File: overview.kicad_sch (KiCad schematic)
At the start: 0 parts

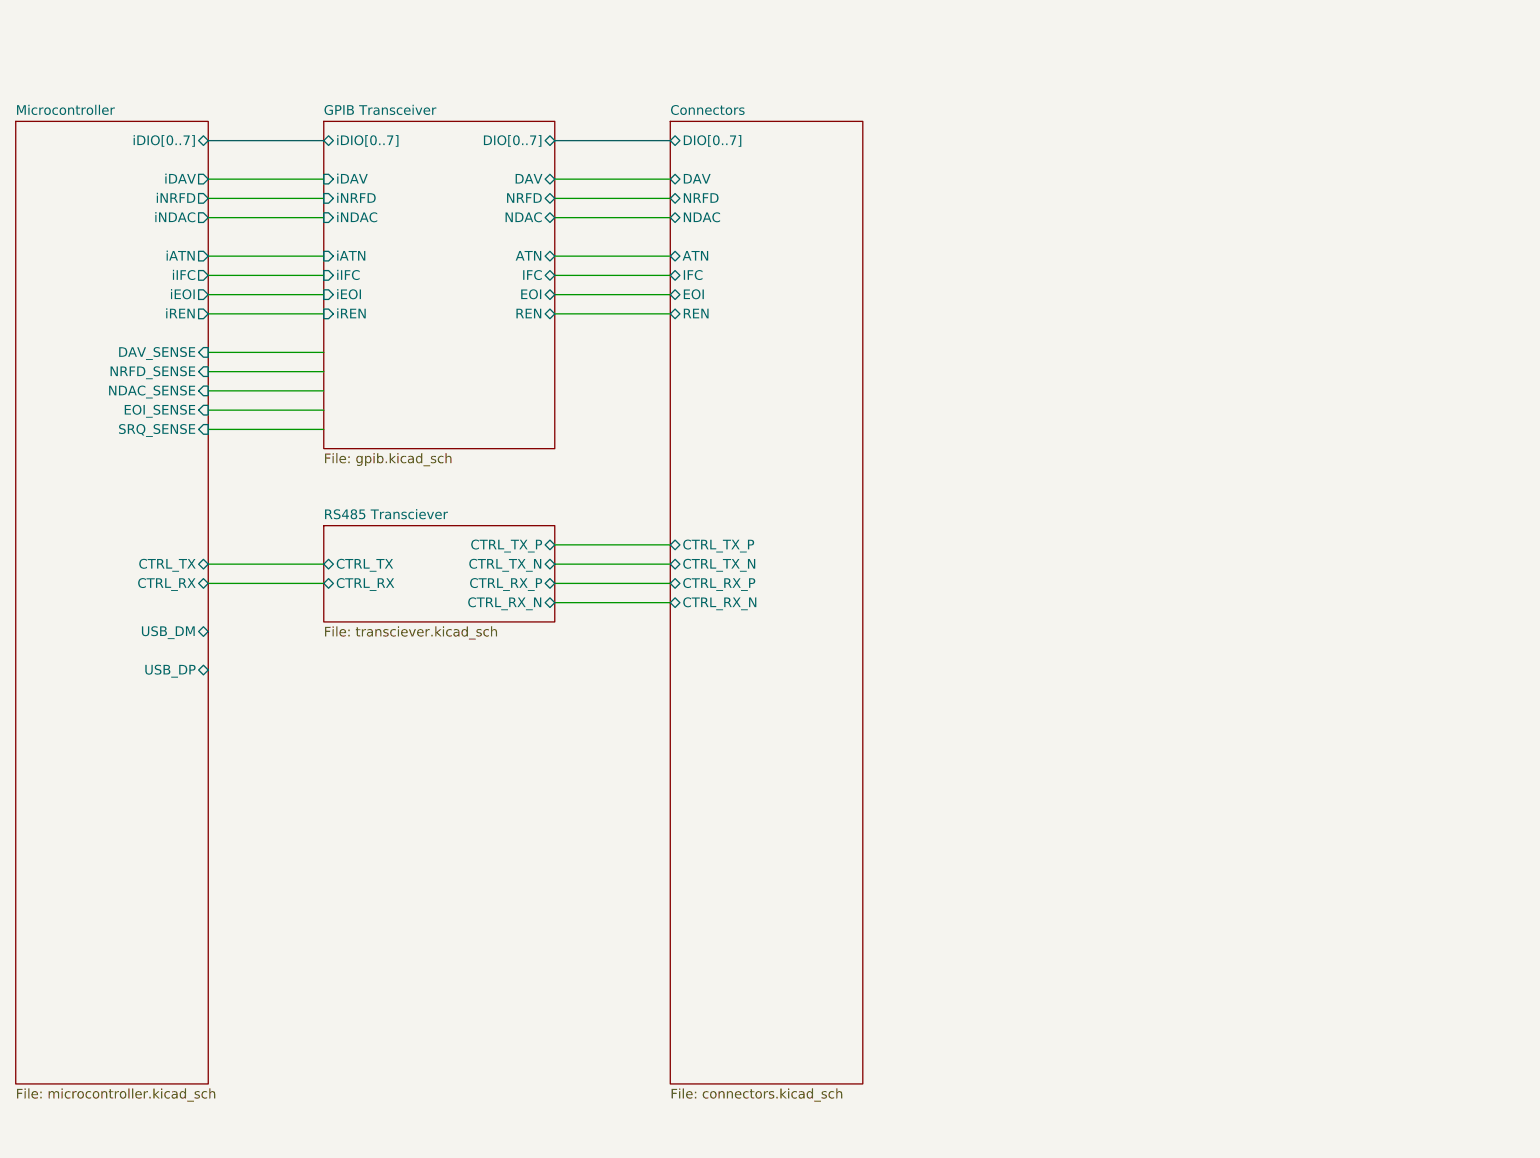
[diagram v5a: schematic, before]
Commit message: Add GPIB interface
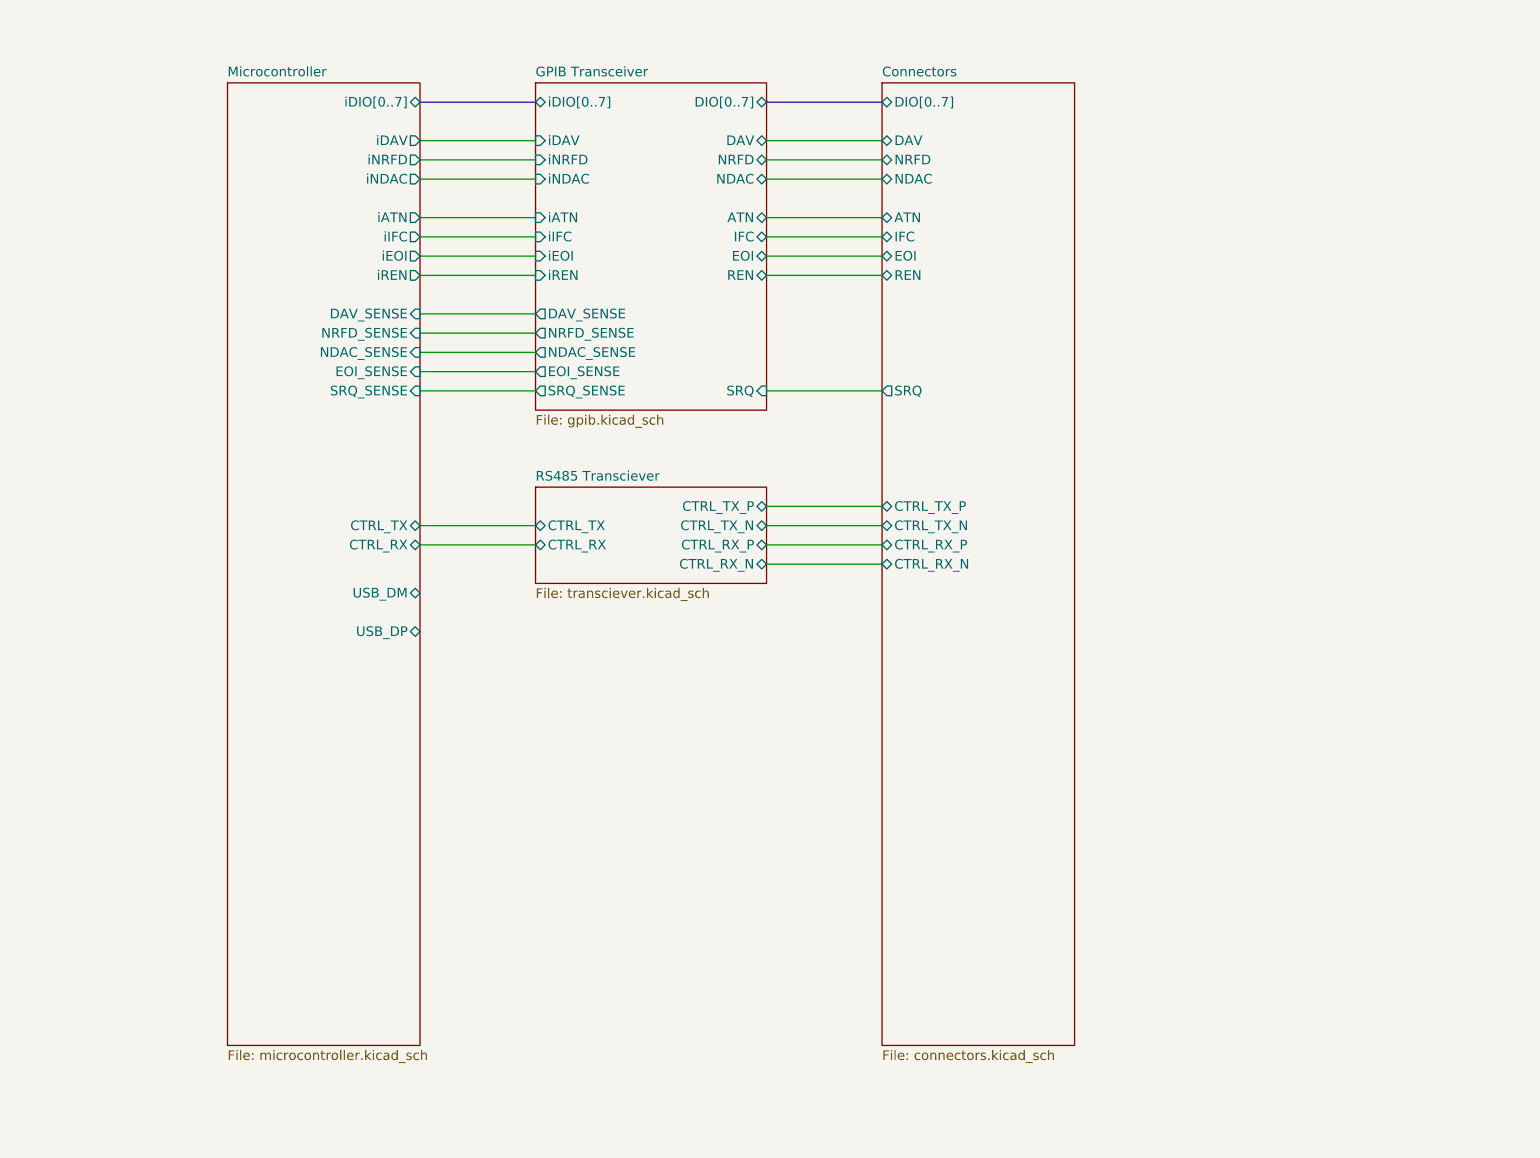
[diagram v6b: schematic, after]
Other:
- sheet Connectors ports: added SRQ; removed none
- sheet GPIB Transceiver ports: added DAV_SENSE, EOI_SENSE, NDAC_SENSE, NRFD_SENSE, SRQ, SRQ_SENSE; removed none

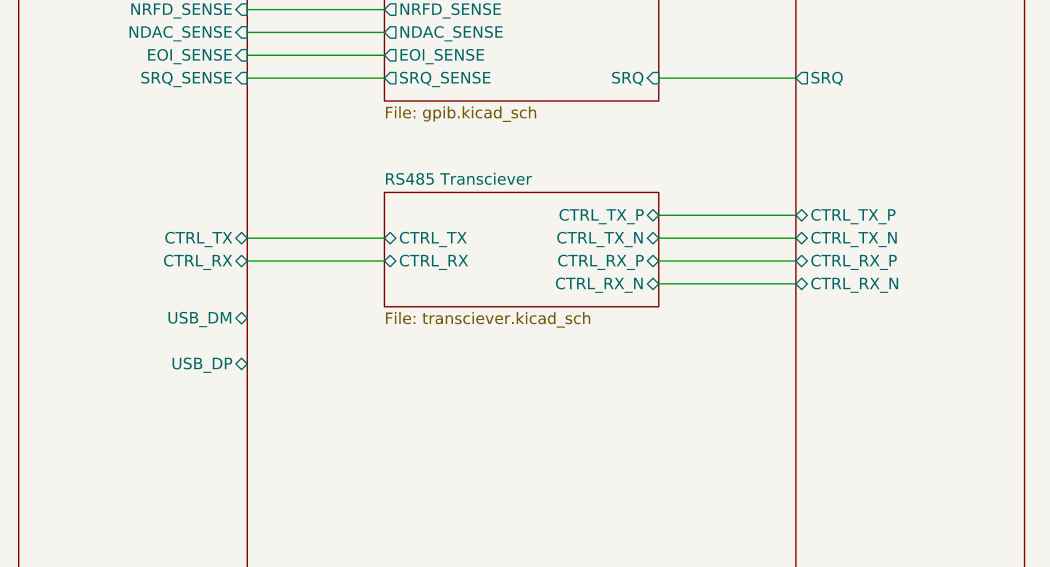
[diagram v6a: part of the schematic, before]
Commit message: Add power supply and USB protection
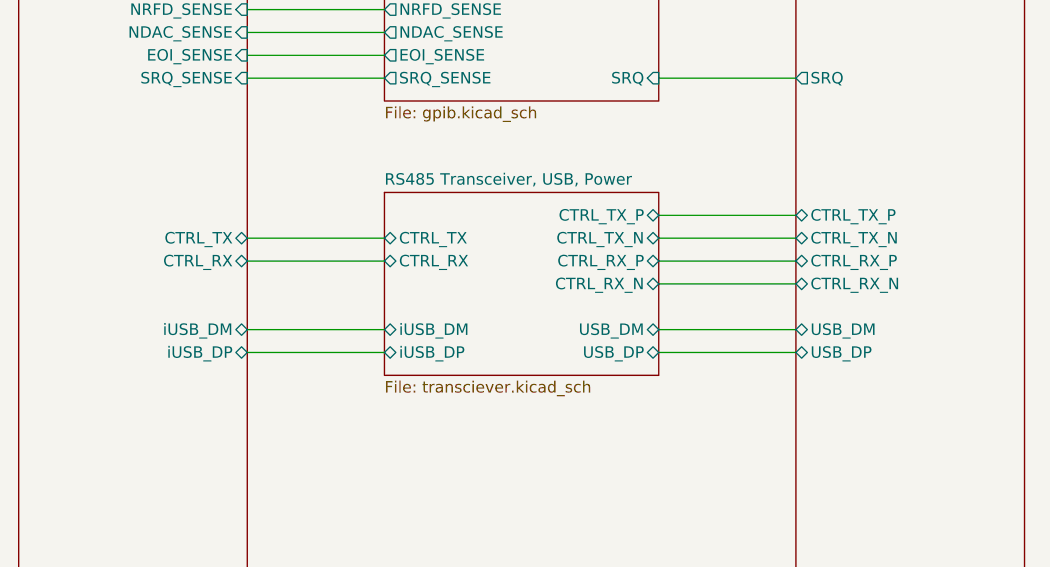
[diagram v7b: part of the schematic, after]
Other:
- sheet RS485 Transciever renamed RS485 Transceiver, USB, Power
- sheet Connectors ports: added USB_DM, USB_DP; removed none
- sheet Microcontroller ports: added iUSB_DM, iUSB_DP; removed USB_DM, USB_DP
- sheet RS485 Transceiver, USB, Power ports: added USB_DM, USB_DP, iUSB_DM, iUSB_DP; removed none
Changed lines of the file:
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@@
+	(wire
+		(pts
+			(xy 180.34 132.08) (xy 195.58 132.08)
+		)
+		(stroke
+			(width 0)
+			(type default)
+		)
+	)
 	(wire
 		(pts
@@
 	(wire
 		(pts
+			(xy 226.06 132.08) (xy 241.3 132.08)
+		)
+		(stroke
+			(width 0)
+			(type default)
+		)
+	)
+	(wire
+		(pts
 			(xy 180.34 71.12) (xy 195.58 71.12)
 		)
@@
 	(wire
 		(pts
+			(xy 180.34 134.62) (xy 195.58 134.62)
+		)
+		(stroke
+			(width 0)
+			(type default)
+		)
+	)
+	(wire
+		(pts
 			(xy 180.34 86.36) (xy 195.58 86.36)
 		)
@@
 		(pts
 			(xy 226.06 127) (xy 241.3 127)
+		)
+		(stroke
+			(width 0)
+			(type default)
+		)
+	)
+	(wire
+		(pts
+			(xy 226.06 134.62) (xy 241.3 134.62)
 		)
 		(stroke
@@
 			)
 		)
-		(pin "USB_DP" bidirectional
-			(at 180.34 135.89 0)
-			(effects
-				(font
-					(size 1.27 1.27)
-				)
-				(justify right)
-			)
-		)
-		(pin "USB_DM" bidirectional
-			(at 180.34 130.81 0)
+		(pin "iUSB_DM" bidirectional
+			(at 180.34 132.08 0)
+			(effects
+				(font
+					(size 1.27 1.27)
+				)
+				(justify right)
+			)
+		)
+		(pin "iUSB_DP" bidirectional
+			(at 180.34 134.62 0)
 			(effects
 				(font
@@
 			)
 		)
+		(pin "USB_DM" bidirectional
+			(at 241.3 132.08 180)
+			(effects
+				(font
+					(size 1.27 1.27)
+				)
+				(justify left)
+			)
+		)
+		(pin "USB_DP" bidirectional
+			(at 241.3 134.62 180)
+			(effects
+				(font
+					(size 1.27 1.27)
+				)
+				(justify left)
+			)
+		)
 		(instances
 			(project "gpib_controller"
@@
 	(sheet
 		(at 195.58 116.84)
-		(size 30.48 12.7)
+		(size 30.48 20.32)
 		(exclude_from_sim no)
 		(in_bom yes)
@@
 			(color 0 0 0 0)
 		)
-		(property "Sheetname" "RS485 Transciever"
+		(property "Sheetname" "RS485 Transceiver, USB, Power"
 			(at 195.58 116.1284 0)
 			(show_name no)
@@
 		)
 		(property "Sheetfile" "transciever.kicad_sch"
-			(at 195.58 130.1246 0)
+			(at 195.58 137.7446 0)
 			(show_name no)
 			(do_not_autoplace no)
@@
 			)
 		)
+		(pin "USB_DM" bidirectional
+			(at 226.06 132.08 0)
+			(effects
+				(font
+					(size 1.27 1.27)
+				)
+				(justify right)
+			)
+		)
+		(pin "USB_DP" bidirectional
+			(at 226.06 134.62 0)
+			(effects
+				(font
+					(size 1.27 1.27)
+				)
+				(justify right)
+			)
+		)
+		(pin "iUSB_DM" bidirectional
+			(at 195.58 132.08 180)
+			(effects
+				(font
+					(size 1.27 1.27)
+				)
+				(justify left)
+			)
+		)
+		(pin "iUSB_DP" bidirectional
+			(at 195.58 134.62 180)
+			(effects
+				(font
+					(size 1.27 1.27)
+				)
+				(justify left)
+			)
+		)

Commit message: Finish up schematics
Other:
- sheet GPIB Transceiver ports: added GPIB_DIR, GPIB_EN; removed none
- sheet Microcontroller ports: added GPIB_DIR, GPIB_EN; removed none
